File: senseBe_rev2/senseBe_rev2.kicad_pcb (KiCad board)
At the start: 2 copper layers, 60 x 40 mm, 51 parts, among them J1 PJ-32434_3-5mmAudioJack, P1 CONN_02X05, Q1 TSM2301, Q2 Q_DUAL_NMOS_DMN2990UDJ-7, Q3 Q_DUAL_NMOS_DMN2990UDJ-7, Q4 Q_DUAL_NMOS_DMN2990UDJ-7, SW1 SW_SPST, SW2 SW_DPST, U1 MDBT42Q, U2 TSSP4056, U3 AP3403, Y1 T38 Mercury

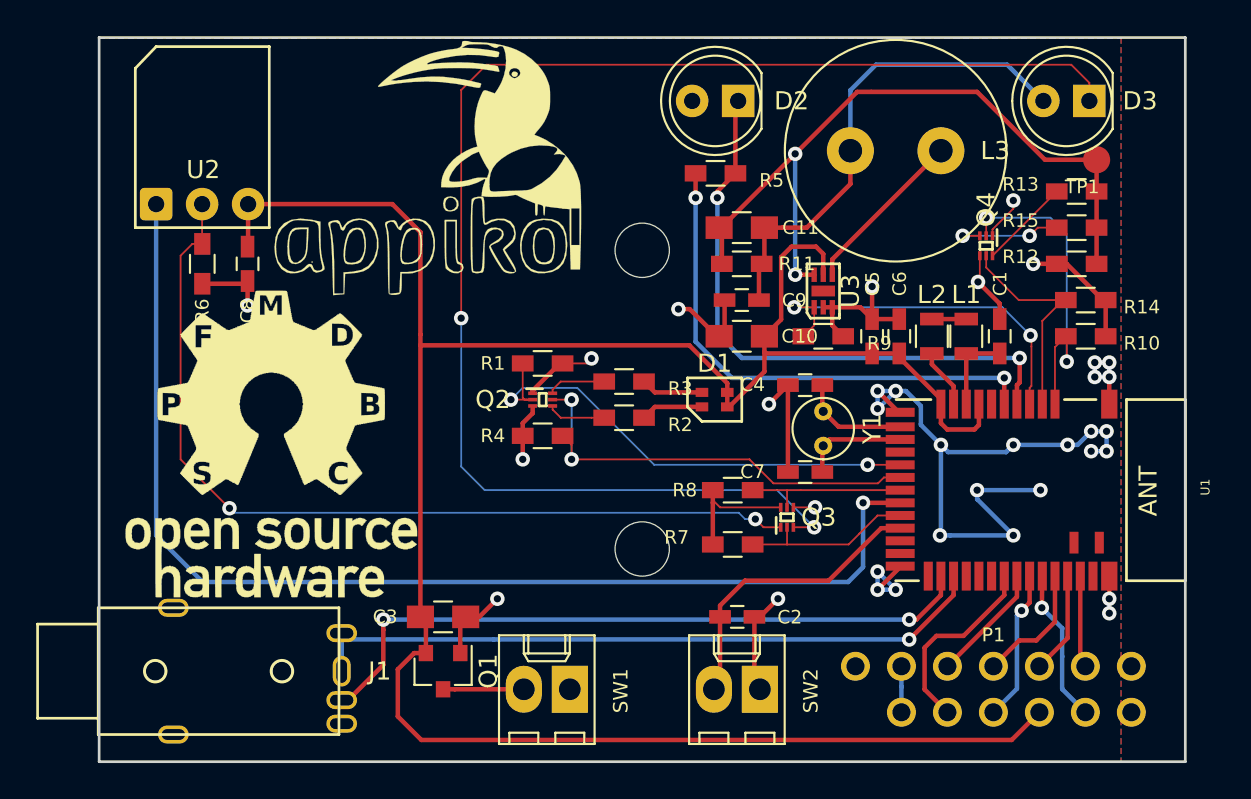
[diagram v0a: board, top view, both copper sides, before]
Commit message: senseBe_rev2 PCB and Gerber files modified.
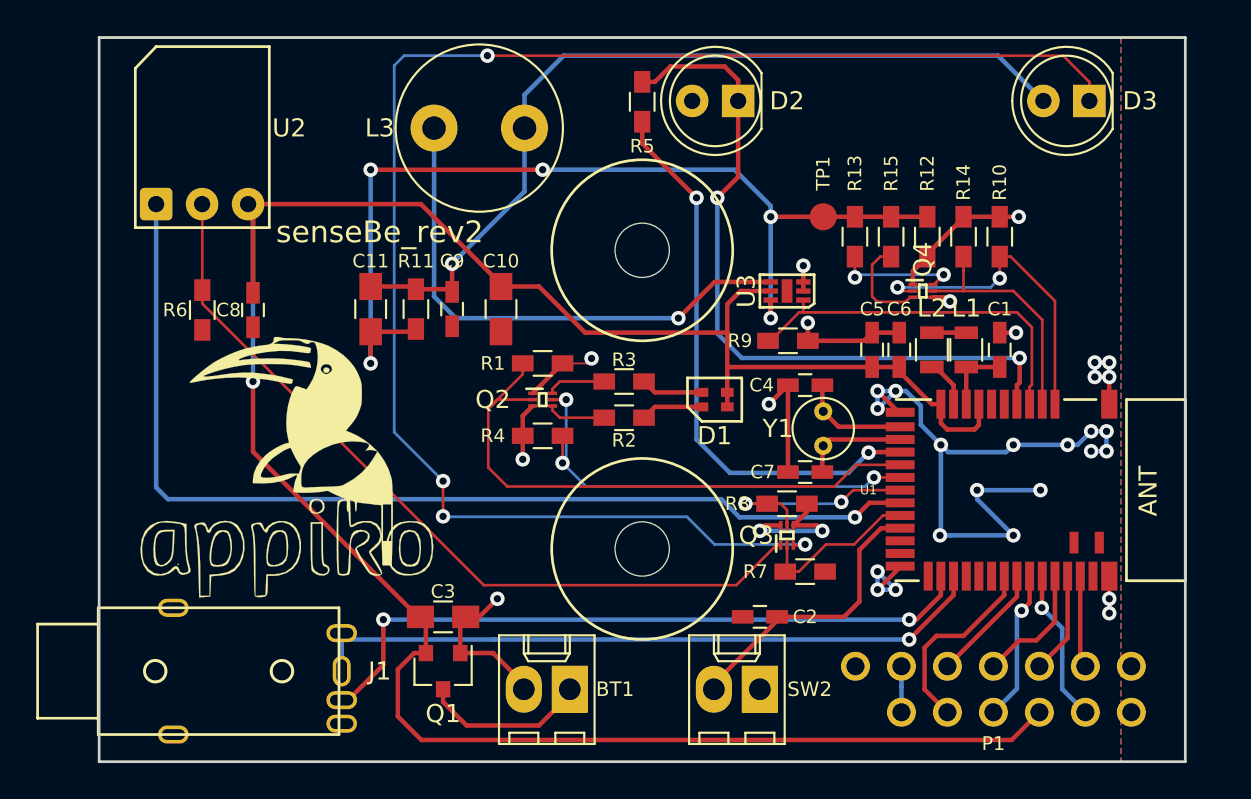
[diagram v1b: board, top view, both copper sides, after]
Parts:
- removed SW1: SW_SPST, senseBe_rev2_fp:Molex_KK-6410-02_02x2.54mm_Straight
- BT1: footprint senseBe_rev2_fp:2462_BatteryHolder_AAx2 -> senseBe_rev2_fp:Molex_KK-6410-02_02x2.54mm_Straight; moved to F.Cu
- G***: moved to B.Cu
- L3: footprint Inductor_THT:L_Radial_D12.0mm_P5.00mm_Fastron_11P -> senseBe_rev2_fp:L_Radial_D12.0mm_P5.00mm_Fastron_11P
- MK1, MK2: footprint MountingHole:MountingHole_3mm -> senseBe_rev2_fp:MountingHole_3mm
- moved G*** 36.7 mm to (46.0, 19.4)
- moved L3 28.0 mm to (18.5, 5.00), turned to 0 degrees
- moved C11 21.0 mm to (15.0, 15.0), turned to 270 degrees
- moved G*** 19.4 mm to (10.6, 22.9)
- moved G*** 18.3 mm to (8.10, 28.2)
- moved R11 18.2 mm to (17.5, 15.0), turned to 270 degrees
- moved BT1 16.5 mm to (26.0, 36.0), turned to 180 degrees
- moved C9 16.0 mm to (19.5, 15.0), turned to 270 degrees
- moved TP1 15.4 mm to (40.0, 9.90), turned to 90 degrees
- moved C10 13.4 mm to (22.2, 15.0), turned to 270 degrees
- moved R13 12.5 mm to (41.8, 11.0), turned to 270 degrees
- moved R15 10.3 mm to (43.8, 11.0), turned to 270 degrees
- moved R12 8.39 mm to (45.8, 11.0), turned to 270 degrees
- moved R14 7.60 mm to (47.8, 11.0), turned to 90 degrees
- moved R10 7.27 mm to (49.8, 11.0), turned to 90 degrees
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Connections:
- Q1 pad 3: Net-(Q1-Pad3) -> Net-(BT1-Pad1)
- U1 pad 15: (no net) -> /LIGHT_SENSE_EN
- U1 pad 6: /LIGHT_SENSE_EN -> (no net)
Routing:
- net /Sheet5C63BFE7/VLED: track 27.1 -> 47.8 mm, vias 0 -> 1
- net Net-(L3-Pad1): track 9.34 -> 29.2 mm, vias 0 -> 1
- net GND: track 114.2 -> 99.9 mm, vias 35 -> 34
- net Net-(C11-Pad2): track 41.0 -> 53.8 mm, vias 2 -> 5
- net Net-(BT1-Pad1): track 0.00 -> 9.24 mm
- net Net-(D3-Pad1): track 79.5 -> 87.6 mm, vias 2 -> 4
- net /LIGHT_SENSE: track 33.2 -> 40.3 mm
- net /RX_OUT: track 64.4 -> 57.8 mm
- net /LED_RED: track 27.2 -> 32.9 mm, vias 2 -> 0
- net VDD: track 125.4 -> 130.3 mm, vias 0 -> 1
- net Net-(Q3-Pad1): track 49.6 -> 44.8 mm, vias 2 -> 0
- net Net-(Q1-Pad3): track 4.46 -> 0.00 mm
- net /IR_LED_EN: track 9.10 -> 12.2 mm, vias 0 -> 2
- net /LIGHT_SENSE_EN: track 28.6 -> 31.3 mm
- net Net-(Q4-Pad6): track 5.02 -> 6.94 mm, vias 0 -> 2
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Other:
- net class Default: trace_width 0.1 -> 0.25
- net class Dual N MOSFET: clearance 0.2 -> 0.1; trace_width 0.1 -> 0.15
- net class Ground added: clearance 0.1, trace_width 0.25, via_dia 0.8, via_drill 0.4
- board text added: "senseBe_rev2"

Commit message: Minor changes of fixing the power Molex connector and traces to Dual MOSFET's SOT963 package.
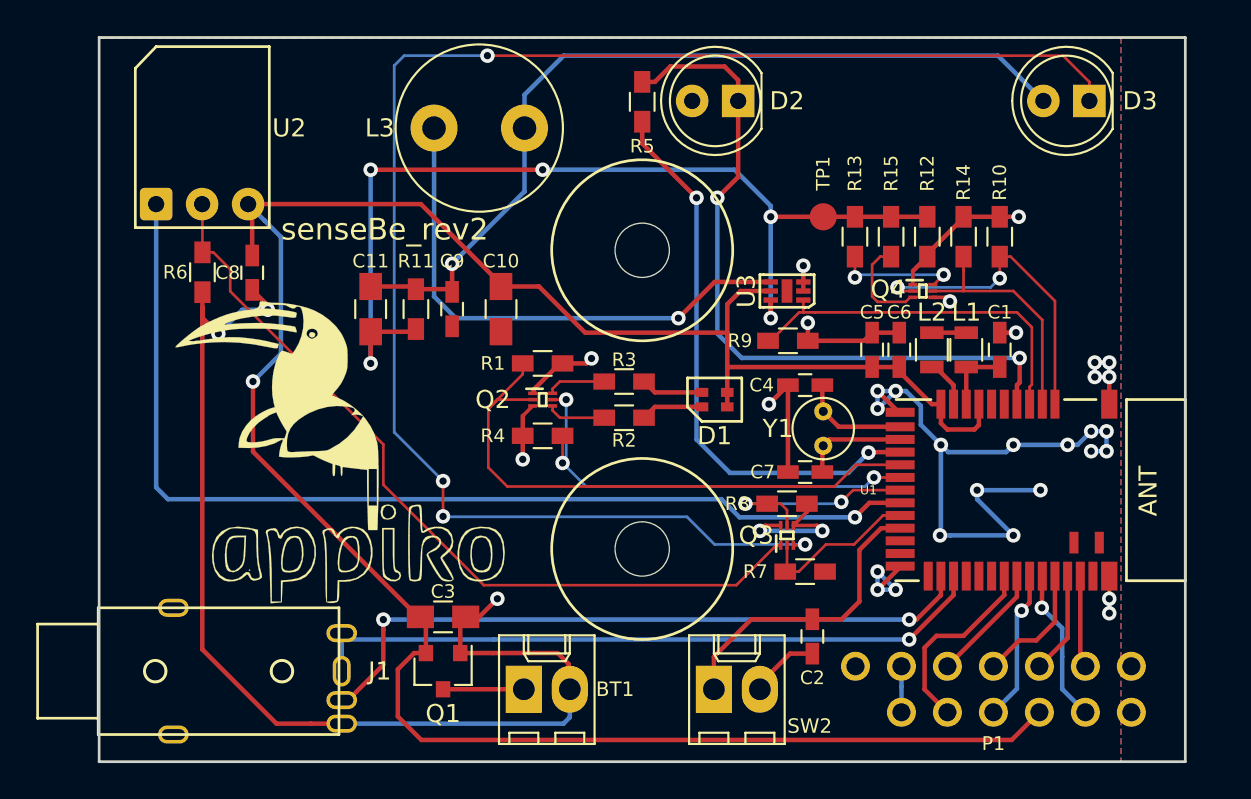
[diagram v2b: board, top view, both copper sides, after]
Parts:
- moved G*** 29.8 mm to (16.3, 19.1), turned to 180 degrees
- moved G*** 3.96 mm to (12.0, 28.5)
- moved C2 3.09 mm to (39.4, 33.1), turned to 90 degrees
- moved G*** 2.11 mm to (9.81, 20.9)
- moved R6 2.09 mm to (5.71, 13.0)
- moved C8 2.06 mm to (8.46, 13.0)
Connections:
- SW2 pad 1: GND -> /BUTTON
- SW2 pad 2: /BUTTON -> GND
- U1 pad 22: (no net) -> Net-(U1-Pad22)
- U1 pad 23: (no net) -> Net-(U1-Pad23)
- U1 pad 25: (no net) -> /CAM_JACK
- U1 pad 28: (no net) -> /UART_JACK
- U1 pad 29: (no net) -> /RX_UARTRX
- U1 pad 30: (no net) -> /RX_UARTTX
- U1 pad 38: (no net) -> Net-(U1-Pad38)
- U1 pad 40: (no net) -> Net-(U1-Pad40)
- U1 pad 41: (no net) -> Net-(U1-Pad41)
- U1 pad 6: (no net) -> Net-(U1-Pad6)
- U1 pad 7: (no net) -> Net-(U1-Pad7)
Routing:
- net GND: track 99.9 -> 157.2 mm, vias 34 -> 36
- net Net-(BT1-Pad1): track 9.24 -> 4.76 mm
- net /BUTTON: track 15.9 -> 17.0 mm
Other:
- rule trace_min: 0.1 -> 0.15
